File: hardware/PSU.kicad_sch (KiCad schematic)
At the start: 19 parts, among them J1 UJ20-C-H-G-SMT-2A-P16-TR, U2 REF35330QDBVR, U4 LM27762, U5 NCP1117-3.3_SOT223

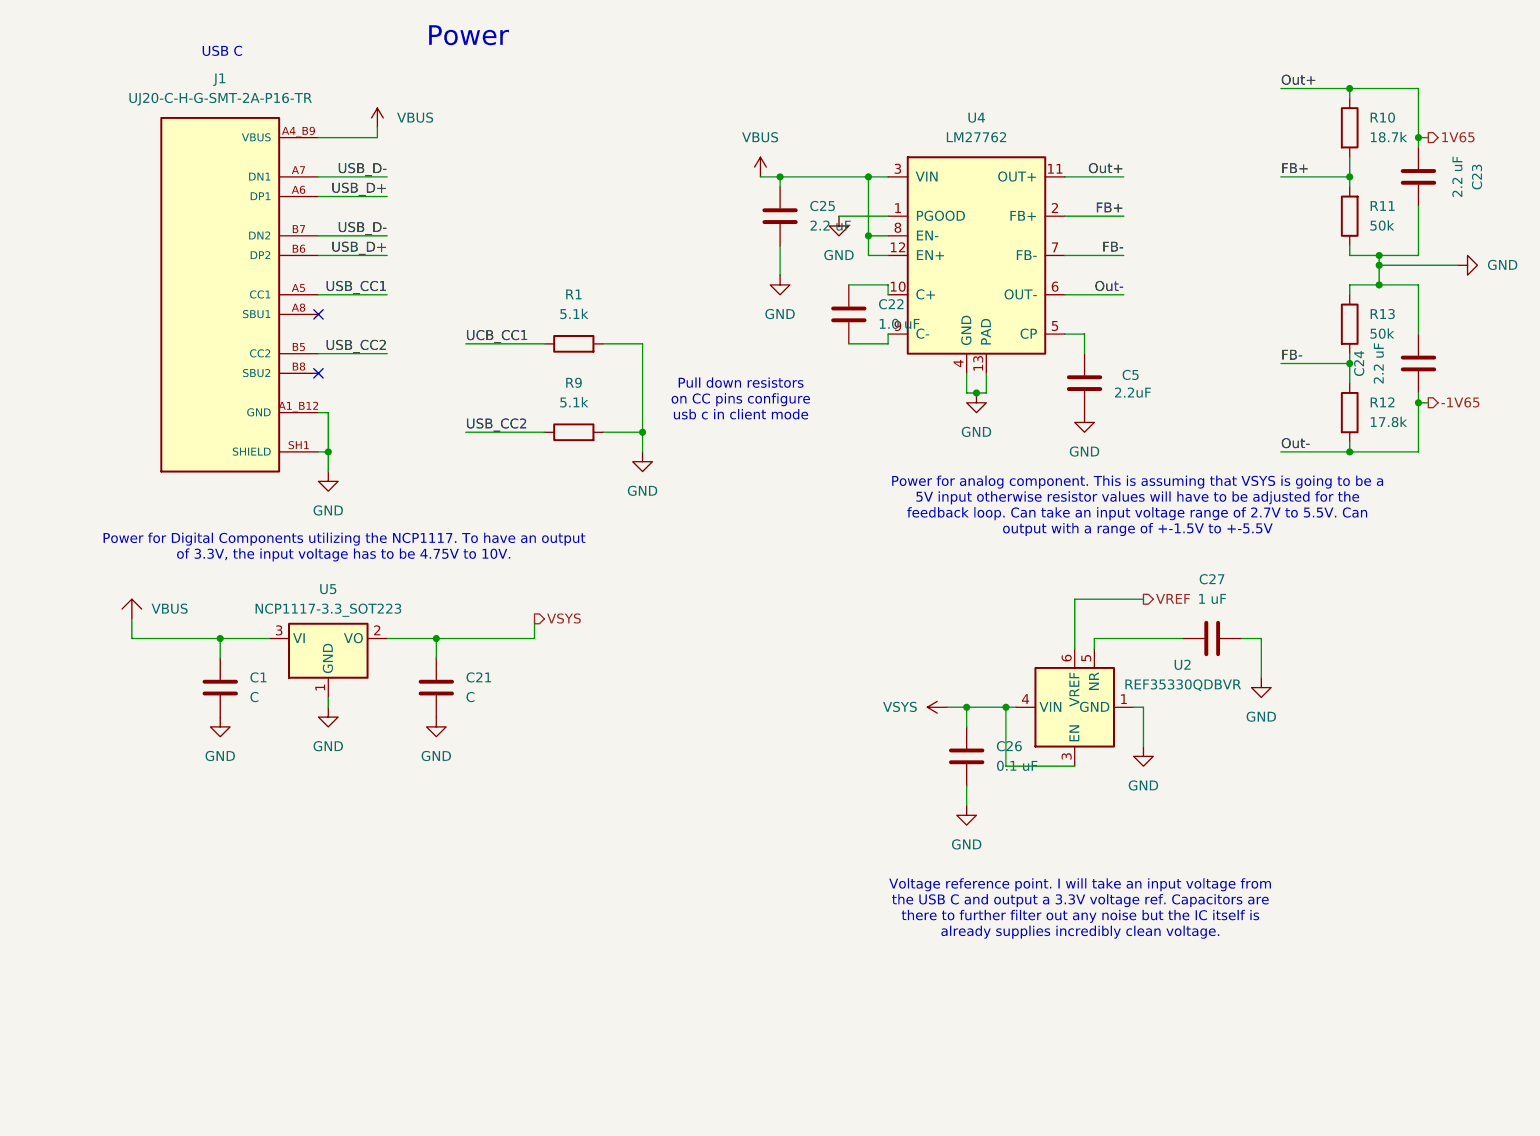
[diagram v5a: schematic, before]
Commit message: connected analog i/o on main schematic and updated PSU naming
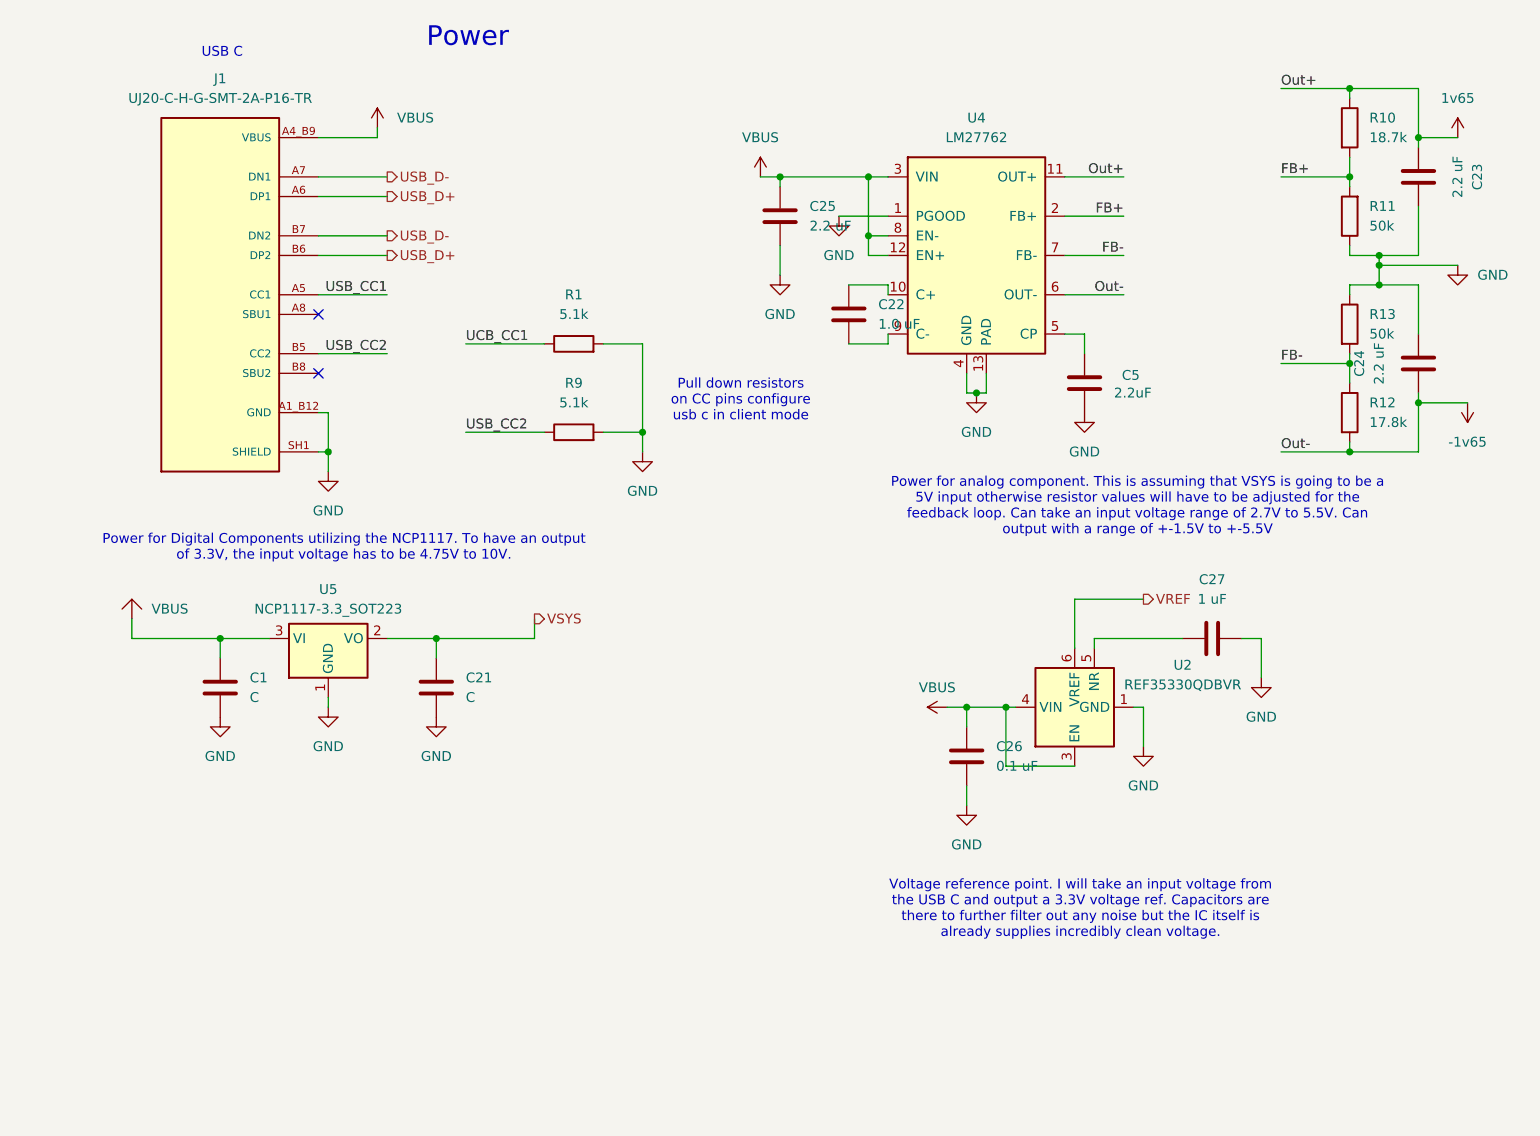
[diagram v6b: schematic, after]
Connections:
- net VBUS: now also C26.1, U2.3 (EN), U2.4 (VIN)
- net VSYS: no longer C26.1, U2.3 (EN), U2.4 (VIN)
- net -1V65 renamed -1v65
- net 1V65 renamed 1v65
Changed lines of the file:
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@@
 	(wire
 		(pts
-			(xy 227.33 82.55) (xy 226.06 82.55)
+			(xy 226.06 82.55) (xy 232.41 82.55)
 		)
 		(stroke
@@
 	(wire
 		(pts
-			(xy 227.33 48.26) (xy 226.06 48.26)
+			(xy 226.06 48.26) (xy 231.14 48.26)
 		)
 		(stroke
@@
 		)
 	)
-	(label "USB_D-"
-		(at 92.71 60.96 180)
-		(effects
-			(font
-				(size 1.27 1.27)
-			)
-			(justify right bottom)
-		)
-	)
 	(label "Out+"
 		(at 208.28 41.91 0)
@@
 		)
 	)
-	(label "USB_D+"
-		(at 92.71 55.88 180)
-		(effects
-			(font
-				(size 1.27 1.27)
-			)
-			(justify right bottom)
-		)
-	)
-	(label "USB_D+"
-		(at 92.71 63.5 180)
-		(effects
-			(font
-				(size 1.27 1.27)
-			)
-			(justify right bottom)
-		)
-	)
 	(label "FB+"
 		(at 187.96 58.42 180)
@@
 		)
 	)
-	(label "USB_D-"
-		(at 92.71 53.34 180)
+	(hierarchical_label "USB_D+"
+		(shape output)
+		(at 92.71 55.88 0)
 		(effects
 			(font
 				(size 1.27 1.27)
 			)
-			(justify right bottom)
+			(justify left)
 		)
 	)
-	(hierarchical_label "-1V65"
+	(hierarchical_label "USB_D+"
 		(shape output)
-		(at 227.33 82.55 0)
+		(at 92.71 63.5 0)
 		(effects
 			(font
@@
 		)
 	)
-	(hierarchical_label "1V65"
+	(hierarchical_label "USB_D-"
+		(shape output)
+		(at 92.71 60.96 0)
+		(effects
+			(font
+				(size 1.27 1.27)
+			)
+			(justify left)
+		)
+	)
+	(hierarchical_label "USB_D-"
 		(shape output)
-		(at 227.33 48.26 0)
+		(at 92.71 53.34 0)
 		(effects
 			(font
@@
 	)
 	(symbol
+		(lib_id "power:VDC")
+		(at 231.14 48.26 0)
+		(unit 1)
+		(exclude_from_sim no)
+		(in_bom yes)
+		(on_board yes)
+		(dnp no)
+		(property "Reference" "#PWR074"
+			(at 231.14 52.07 0)
+			(effects
+				(font
+					(size 1.27 1.27)
+				)
+				(hide yes)
+			)
+		)
+		(property "Value" "1v65"
+			(at 231.14 43.18 0)
+			(effects
+				(font
+					(size 1.27 1.27)
+				)
+			)
+		)
+		(property "Footprint" ""
+			(at 231.14 48.26 0)
+			(effects
+				(font
+					(size 1.27 1.27)
+				)
+				(hide yes)
+			)
+		)
+		(property "Datasheet" ""
+			(at 231.14 48.26 0)
+			(effects
+				(font
+					(size 1.27 1.27)
+				)
+				(hide yes)
+			)
+		)
+		(property "Description" "Power symbol creates a global label with name \"VDC\""
+			(at 231.14 48.26 0)
+			(effects
+				(font
+					(size 1.27 1.27)
+				)
+				(hide yes)
+			)
+		)
+		(pin "1"
+		)
+		(instances
+			(project "RP2350_60QFN_minimal"
+				(path "/94683f5c-9cd9-448e-be96-9792537b5cb8/6296dfbc-bf5e-4649-b078-009c1ac21de6"
+					(reference "#PWR074")
+					(unit 1)
+				)
+			)
+		)
+	)
+	(symbol
 		(lib_name "GND_3")
 		(lib_id "power:GND")
@@
 	(symbol
 		(lib_id "power:GND")
-		(at 231.14 64.77 90)
+		(at 231.14 64.77 0)
 		(unit 1)
 		(exclude_from_sim no)
@@
 		(fields_autoplaced yes)
 		(property "Reference" "#PWR029"
-			(at 237.49 64.77 0)
+			(at 231.14 71.12 0)
 			(effects
 				(font
@@
 		)
 		(property "Value" "GND"
-			(at 234.95 64.7699 90)
+			(at 233.68 66.0399 0)
 			(effects
 				(font
 					(size 1.27 1.27)
 				)
-				(justify right)
+				(justify left)
 			)
 		)
@@
 	)
 	(symbol
+		(lib_id "power:VDC")
+		(at 232.41 82.55 180)
+		(unit 1)
+		(exclude_from_sim no)
+		(in_bom yes)
+		(on_board yes)
+		(dnp no)
+		(property "Reference" "#PWR073"
+			(at 232.41 78.74 0)
+			(effects
+				(font
+					(size 1.27 1.27)
+				)
+				(hide yes)
+			)
+		)
+		(property "Value" "-1v65"
+			(at 232.41 87.63 0)
+			(effects
+				(font
+					(size 1.27 1.27)
+				)
+			)
+		)
+		(property "Footprint" ""
+			(at 232.41 82.55 0)
+			(effects
+				(font
+					(size 1.27 1.27)
+				)
+				(hide yes)
+			)
+		)
+		(property "Datasheet" ""
+			(at 232.41 82.55 0)
+			(effects
+				(font
+					(size 1.27 1.27)
+				)
+				(hide yes)
+			)
+		)
+		(property "Description" "Power symbol creates a global label with name \"VDC\""
+			(at 232.41 82.55 0)
+			(effects
+				(font
+					(size 1.27 1.27)
+				)
+				(hide yes)
+			)
+		)
+		(pin "1"
+		)
+		(instances
+			(project "RP2350_60QFN_minimal"
+				(path "/94683f5c-9cd9-448e-be96-9792537b5cb8/6296dfbc-bf5e-4649-b078-009c1ac21de6"
+					(reference "#PWR073")
+					(unit 1)
+				)
+			)
+		)
+	)
+	(symbol
 		(lib_name "GND_10")
 		(lib_id "power:GND")
@@
 			)
 		)
-		(property "Value" "VSYS"
-			(at 161.29 121.9199 90)
+		(property "Value" "VBUS"
+			(at 163.83 119.38 90)
 			(effects
 				(font
 					(size 1.27 1.27)
 				)
-				(justify left)
 			)
 		)

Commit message: feat(hardware): Cleanup schematic, replace offset stage with non-inverting op amp, add neopixel LED
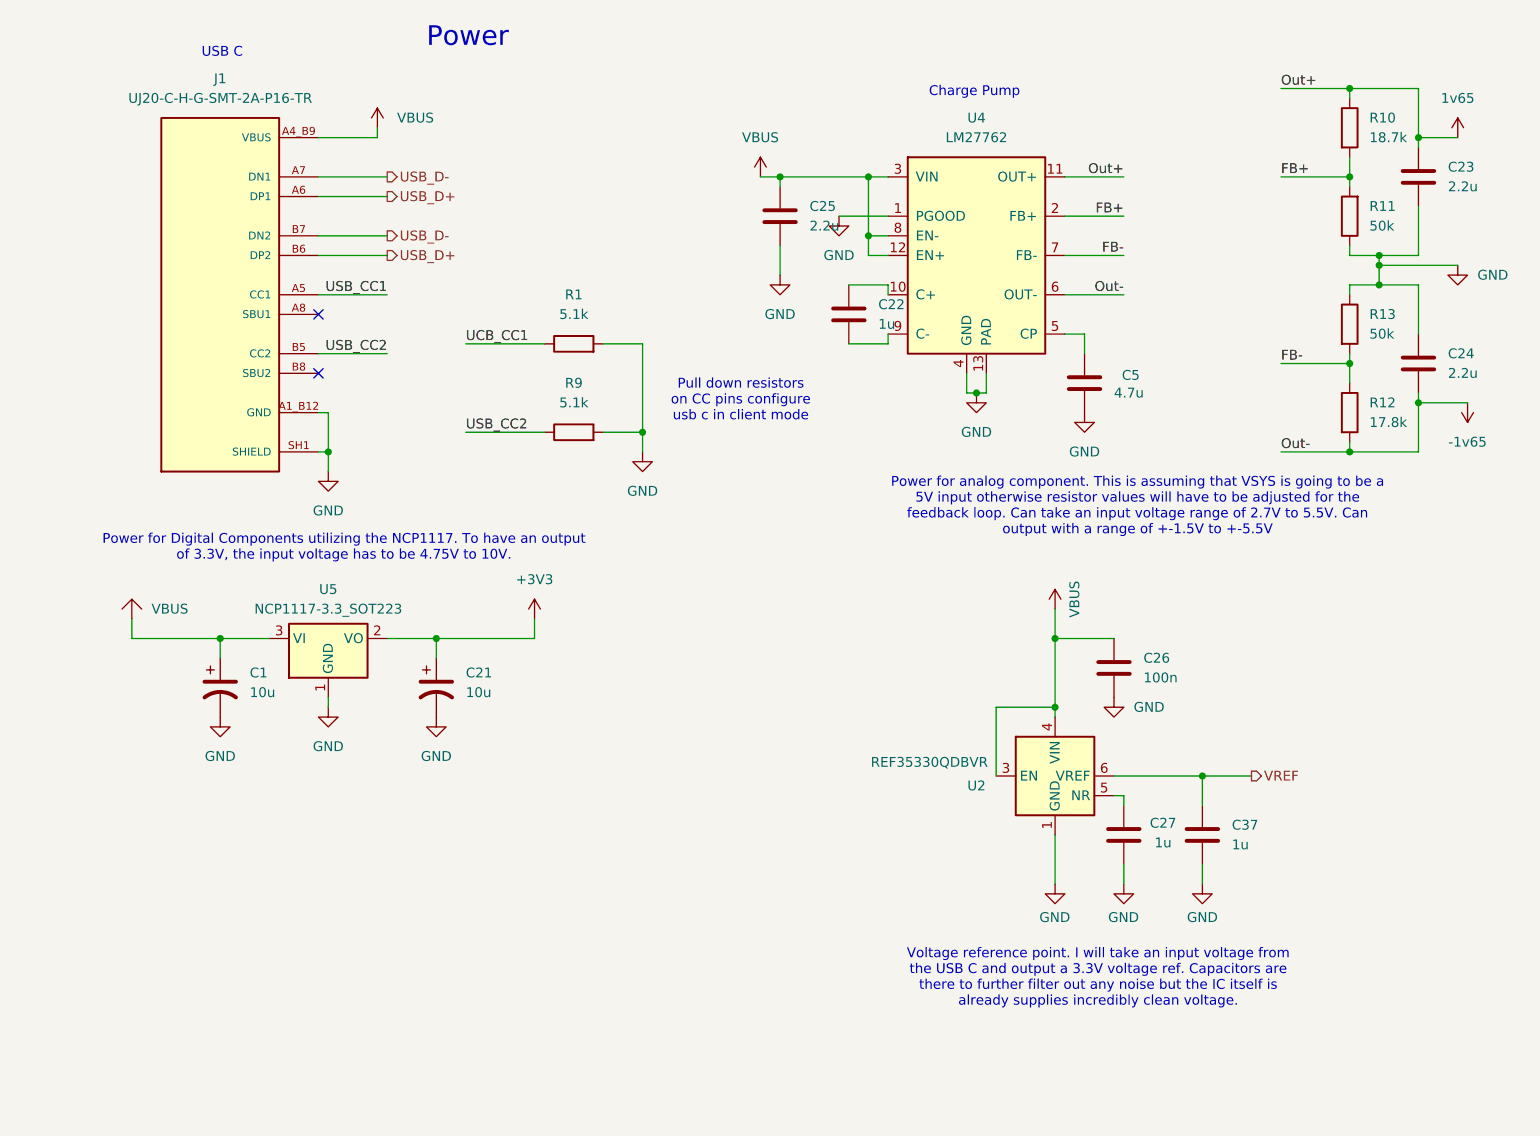
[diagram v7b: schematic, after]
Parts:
- removed C1, C21: C, symbol Device:C
- added C1, C21: 10u, symbol Device:C_Polarized_US
- added C37: 1u, symbol Device:C
- C22: value 1.0 uF -> 1u
- C23, C24, C25: value 2.2 uF -> 2.2u
- C26: value 0.1 uF -> 100n
- C27: value 1 uF -> 1u
- C5: value 2.2uF -> 4.7u
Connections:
- net GND: now also C1.2, C21.2, C37.2
- net VBUS: now also C1.1
- net VREF: now also C37.1
- net VSYS renamed +3V3
- net +3V3: now also C21.1
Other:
- note added: "Charge Pump"
- moved on the sheet: C26, C27, U2

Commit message: feat(hardware): Add charge pump over-voltage protection
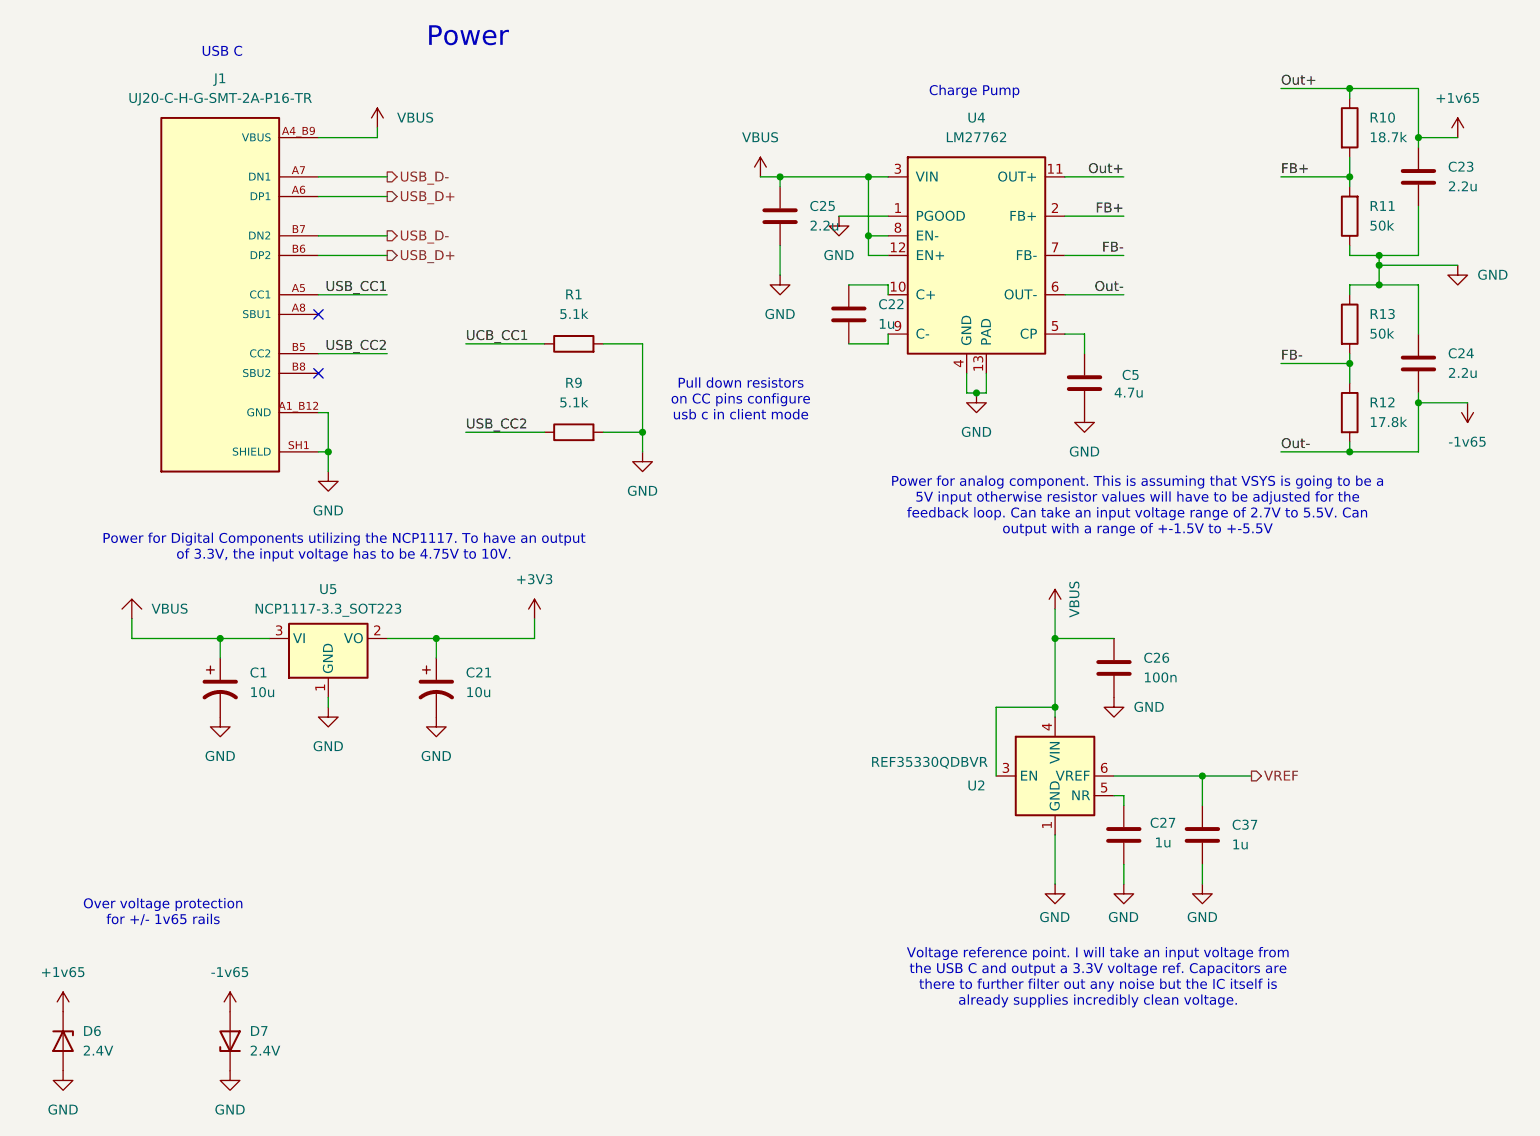
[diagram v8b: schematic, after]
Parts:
- added D6, D7: 2.4V, symbol Device:D_Zener
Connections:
- net -1v65: now also D7.2 (A)
- net GND: now also D6.2 (A), D7.1 (K)
- net 1v65 renamed +1v65
- net +1v65: now also D6.1 (K)
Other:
- note added: "Over voltage protection for +/- 1v65 rails"
